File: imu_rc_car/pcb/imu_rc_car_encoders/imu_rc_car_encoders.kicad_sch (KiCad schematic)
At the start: 24 parts, among them J1 Conn_01x04_Socket, U2 LMV393, U3 ITR9608-F, U4 ITR9608-F

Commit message: commit #17
IR Speed Encoder board v1.0
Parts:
- removed C6: 100nF, Capacitor_SMD:C_0805_2012Metric, symbol Device:C
- removed D2: PMEG2010ER, Diode_SMD:Nexperia_CFP3_SOD-123W, symbol Diode:PMEG2010ER
- removed U2: LMV393, Package_SO:SOIC-8_3.9x4.9mm_P1.27mm, symbol Comparator:LMV393
- removed U3, U4: ITR9608-F, OptoDevice:Everlight_ITR9608-F, symbol Sensor_Proximity:ITR9608-F
- added U1, U2: ITR9608-F, OptoDevice:Everlight_ITR9608-F, symbol Sensor_Proximity:ITR9608-F
- added U3: LMV393, Package_SO:SOIC-8_3.9x4.9mm_P1.27mm, symbol Comparator:LMV393
- C1, C2: value 100nF -> 1nF
- C4: value 10uF -> 100nF
- C7: value 100nF -> 10uF
- J1: footprint Connector_JST:JST_PH_S4B-PH-K_1x04_P2.00mm_Horizontal -> Connector_JST:JST_PH_S4B-PH-SM4-TB_1x04-1MP_P2.00mm_Horizontal
- R2: value 10k -> 180
- R6: value 180 -> 10k
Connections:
- net +3.3V: now also C5.1, C7.1, J1.1 (Pin_1), R11.2, R4.1, R9.1, U3.8 (V+); no longer C1.1, C4.1, C7.2, R6.1, R8.1
- net ENC1: now also R9.2, U3.1; no longer R5.2
- net ENC2: now also U3.7
- net GND: now also C7.2, R6.2, R8.2, U1.2, U1.3, U2.2, U2.3, U3.4 (V-); no longer R4.2, R9.2
- net at R1.2: now also U1.1
- net at C3.1: now also C1.1, R3.2, U1.4, U3.3 (+); no longer R7.2
- new net: R2.2, U2.1
- new net: R5.2, R6.1, U3.2 (-)
- new net: C2.1, C4.1, R4.2, U2.4, U3.5 (+)
- new net: R7.2, R8.1, U3.6 (-)

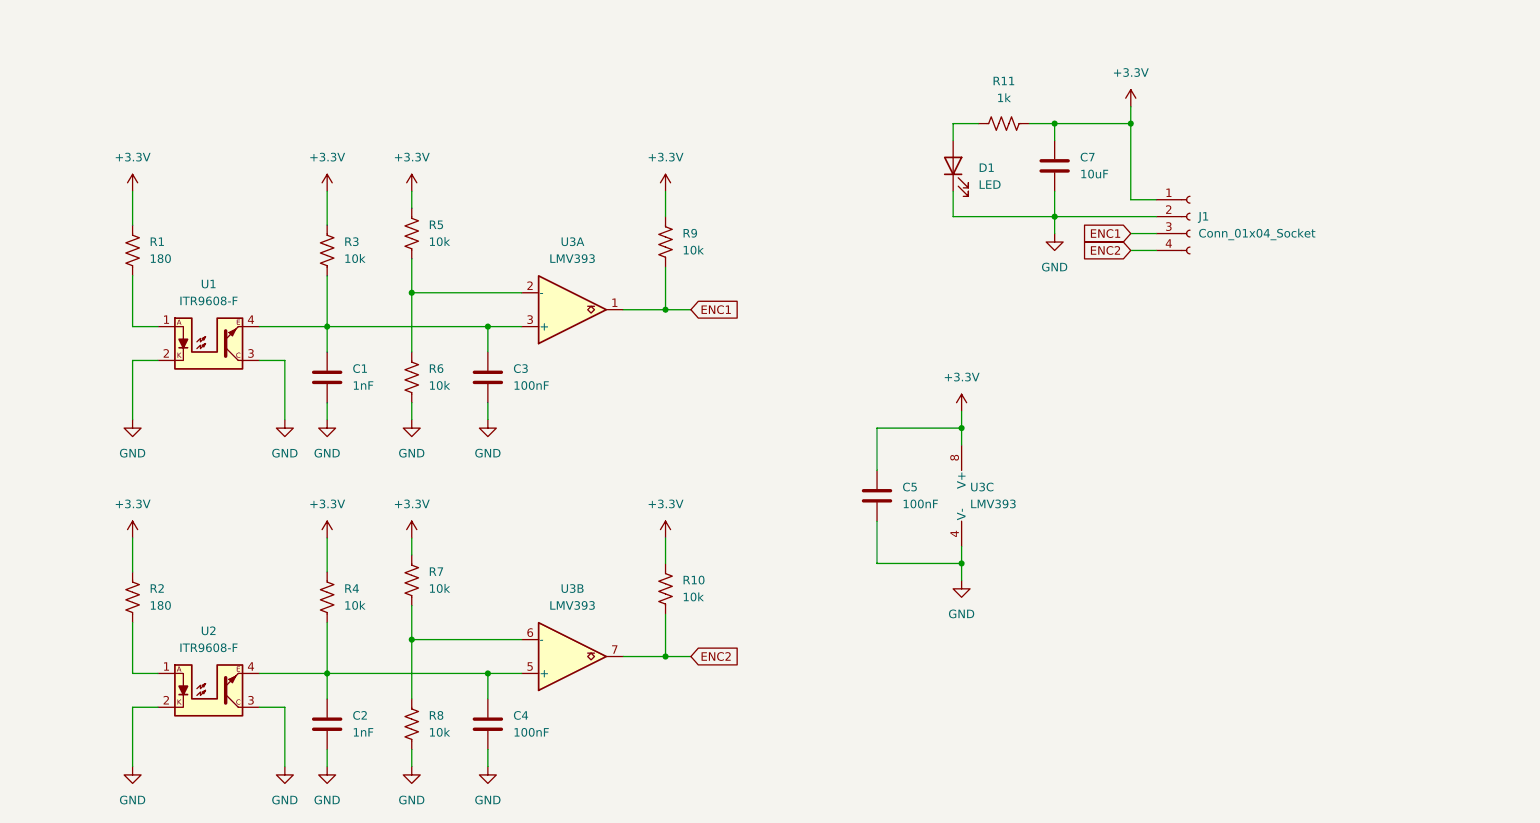
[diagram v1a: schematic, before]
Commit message: commit #20
Proximity Sensor Board v1.0.0
minor tweaks to encoder board
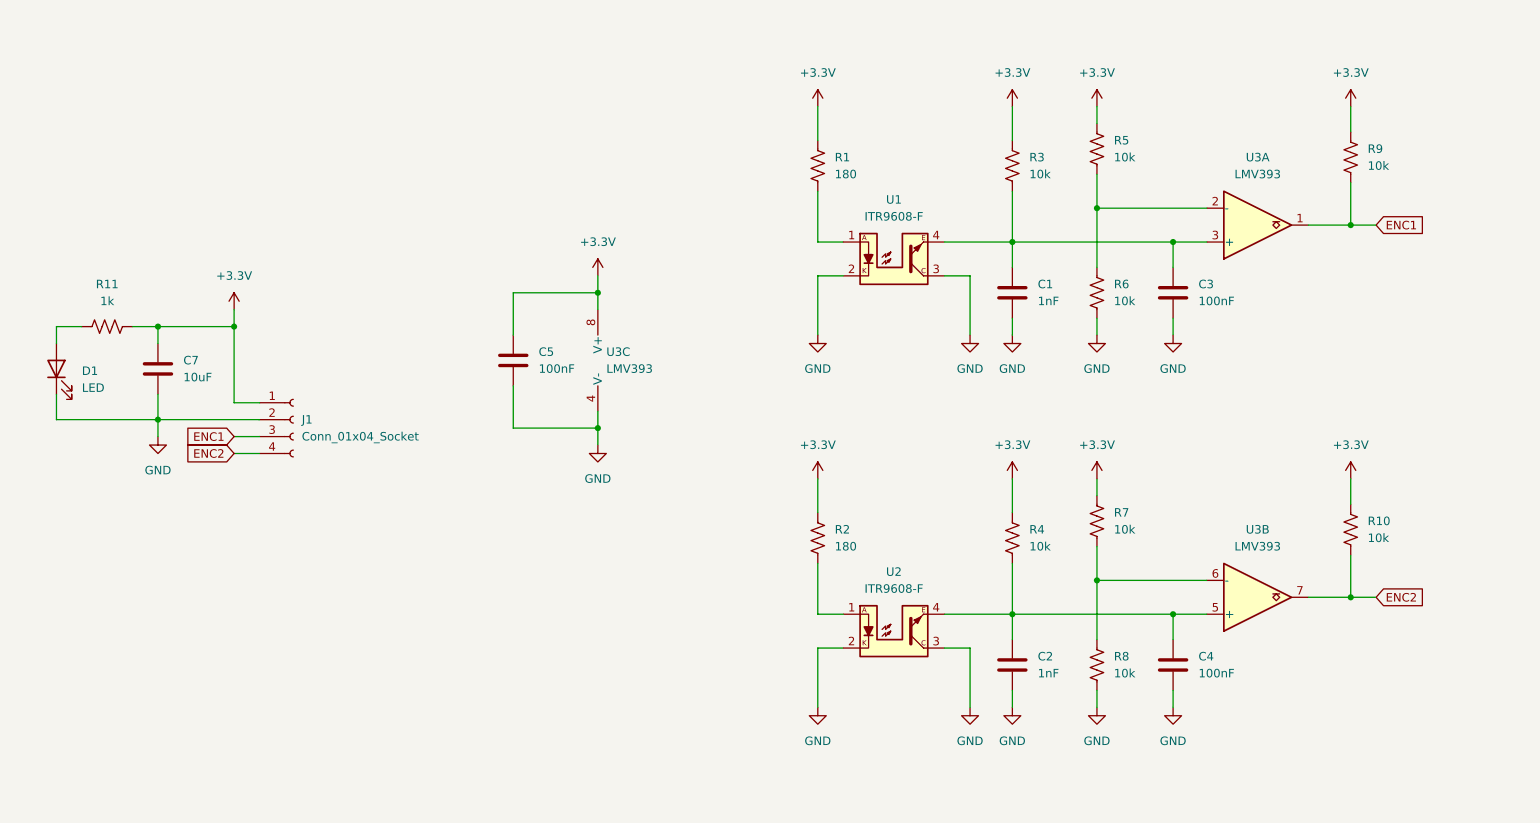
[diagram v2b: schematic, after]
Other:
- moved on the sheet: C1, C2, C3, C4, C5, C7, D1, J1, R1, R10, R11, R2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

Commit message: commit #21
changed some dimensions in 3D chassis model
added 3D standoff
added 3D support side motors
backup files are now removed to reduce clutter

IR RPM Encoder Board v1.1.0
changed some dimensions
better layout for JLCPCB
better stitching

src code:
major changes regarding timers and update ticks
refactored all header functions to separate cpp files
refactored pre-compiler lines
better readability
refactored some oled lines
interrupt function buttons have been added
minor changes to led behaviour
data read and send data are now separate processes
bug fix in car stop
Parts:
- J1: footprint Connector_JST:JST_PH_S4B-PH-SM4-TB_1x04-1MP_P2.00mm_Horizontal -> IMURCLibrary:JST_PH_S4B-PH-SM4-TB_1x04-1MP_P2.00mm_Horizontal
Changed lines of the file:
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@@
 			)
 		)
-		(property "Footprint" "Connector_JST:JST_PH_S4B-PH-SM4-TB_1x04-1MP_P2.00mm_Horizontal"
+		(property "Footprint" "IMURCLibrary:JST_PH_S4B-PH-SM4-TB_1x04-1MP_P2.00mm_Horizontal"
 			(at 63.5 91.44 0)
 			(effects

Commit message: commit #27
revision for hand unit complete (board is ready)
board for proximity sensors in series
minor revision in encoder board
progressing work in car board
added essential libraries support for 3D components
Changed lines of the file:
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@@
 (kicad_sch
-	(version 20231120)
+	(version 20250114)
 	(generator "eeschema")
-	(generator_version "8.0")
+	(generator_version "9.0")
 	(paper "A4")
 	(junction
@@
 		)
 	)
+	(embedded_fonts no)
 )

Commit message: commit #30
changed 3d model offset in esp32s3
imported mouse-bites to kicad
final changes in imu-rc car before revision
critical change in pins 3 and 4 of optical sensor which were switched (encoder board)
removed test unit
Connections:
- net GND: now also U1.4, U2.4; no longer U1.3, U2.3
- net at C1.1, C3.1, R3.2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: now also U1.3; no longer U1.4
- net at C2.1, C4.1, R4.2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: now also U2.3; no longer U2.4
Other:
- moved on the sheet: C1, C2, C3, C4, C5, C7, D1, J1, R1, R10, R11, R2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
